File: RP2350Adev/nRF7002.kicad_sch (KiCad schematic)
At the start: 32 parts, among them U3 LFD_Diplexer, U4 nRF7002-QFAA, X3 XTAL-40

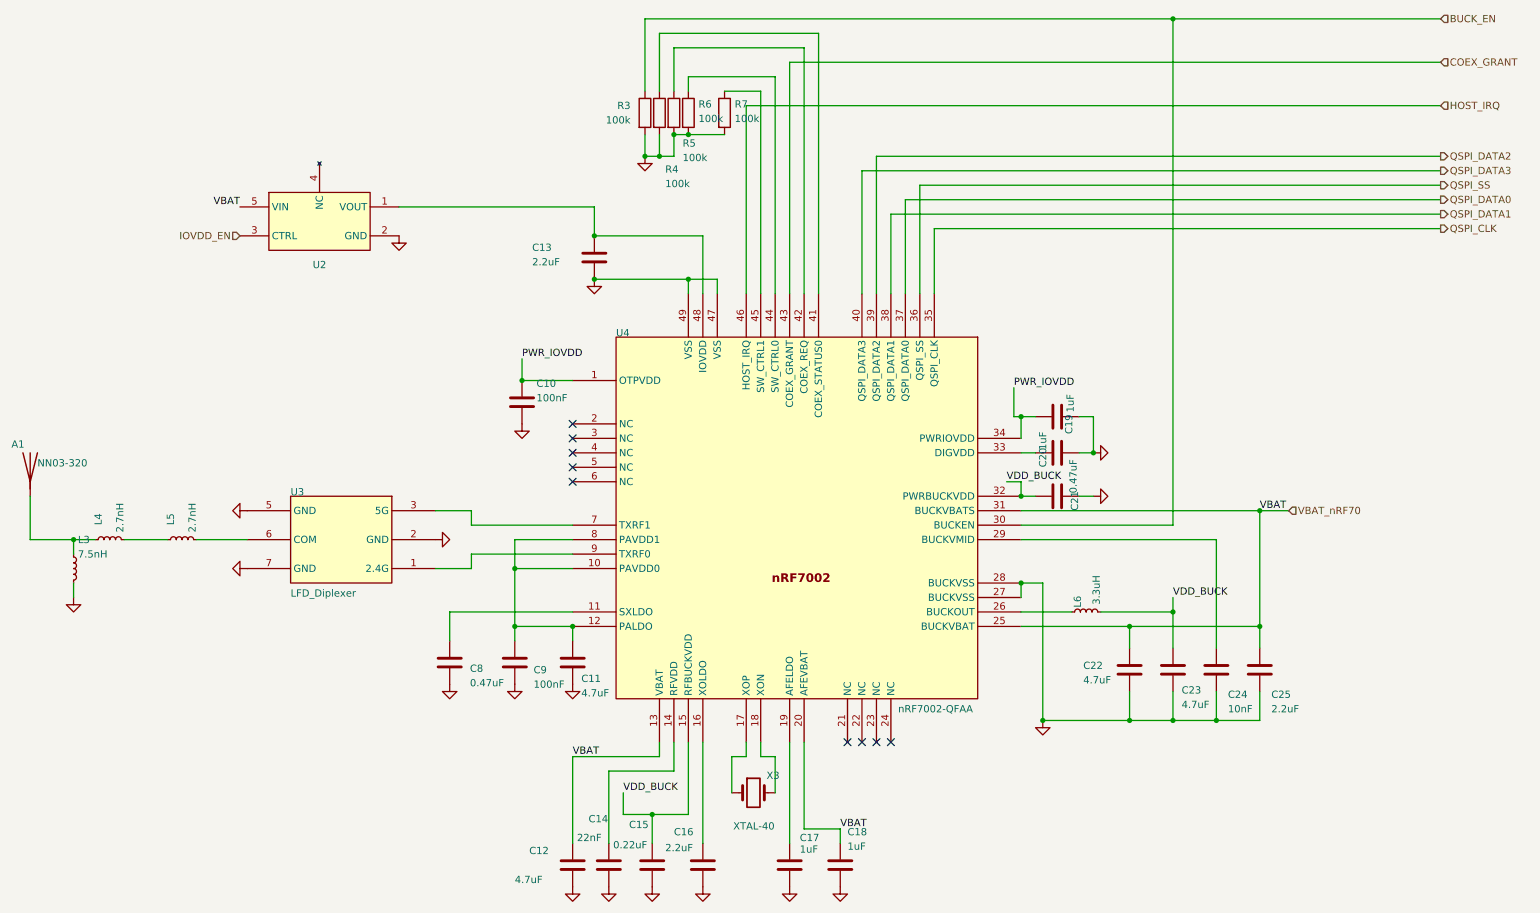
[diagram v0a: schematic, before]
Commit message: Layout Assembly Attempt (Components not being transferred as expected, major issues)
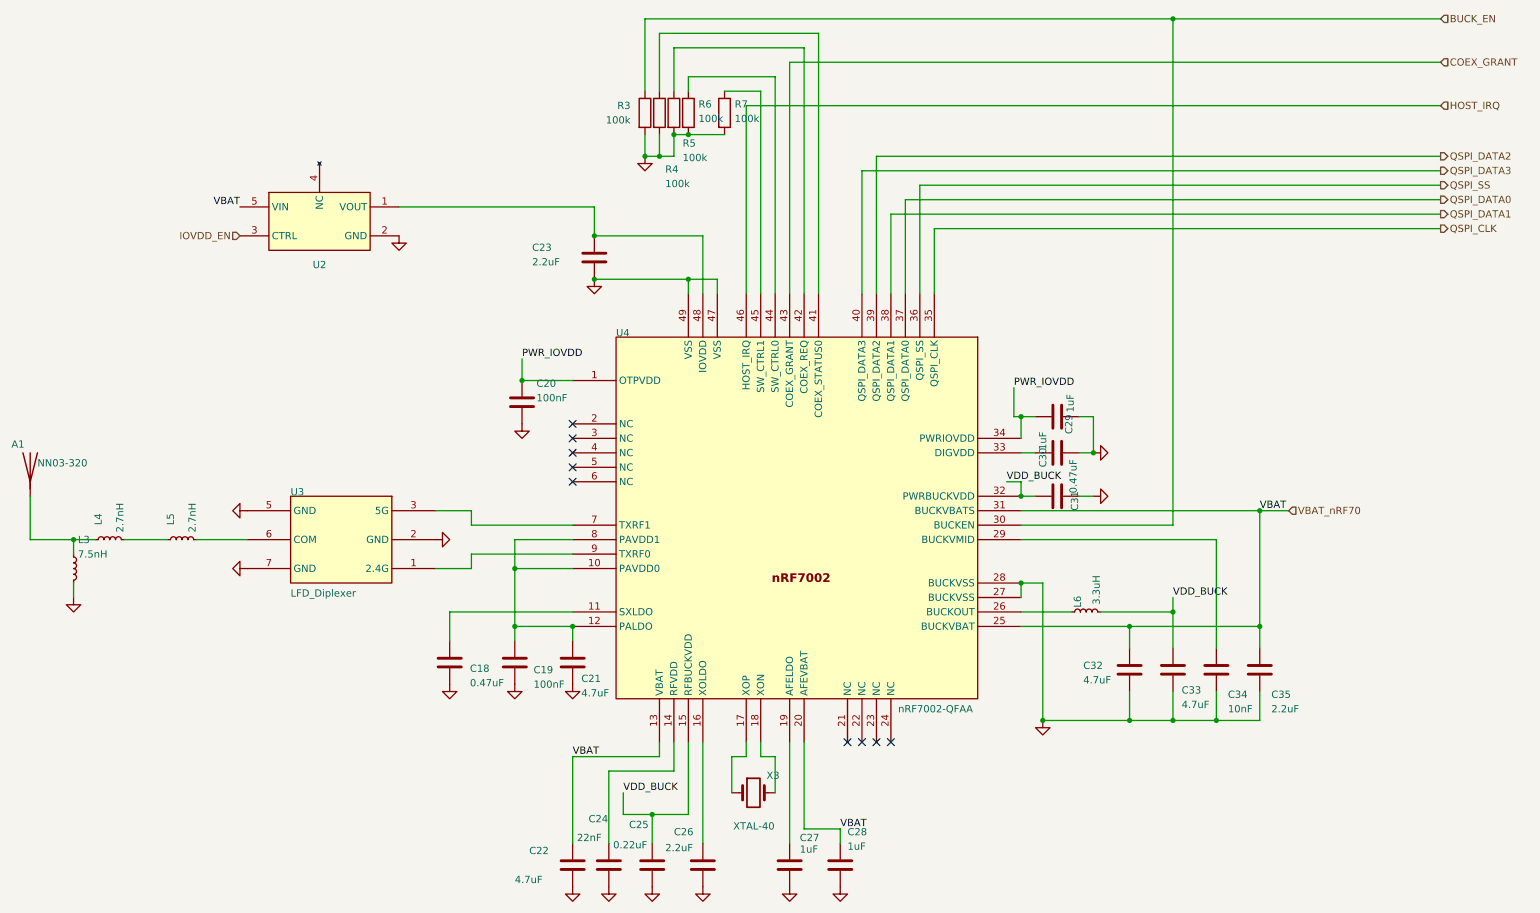
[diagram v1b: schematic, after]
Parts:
- renumbered C8 to C18, C9 to C19, C10 to C20, C11 to C21, C12 to C22, C13 to C23, C14 to C24, C15 to C25, C16 to C26, C17 to C27, C18 to C28, C19 to C29, C20 to C30, C21 to C31, C22 to C32, C23 to C33, C24 to C34, C25 to C35

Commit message: Combine subcircuits
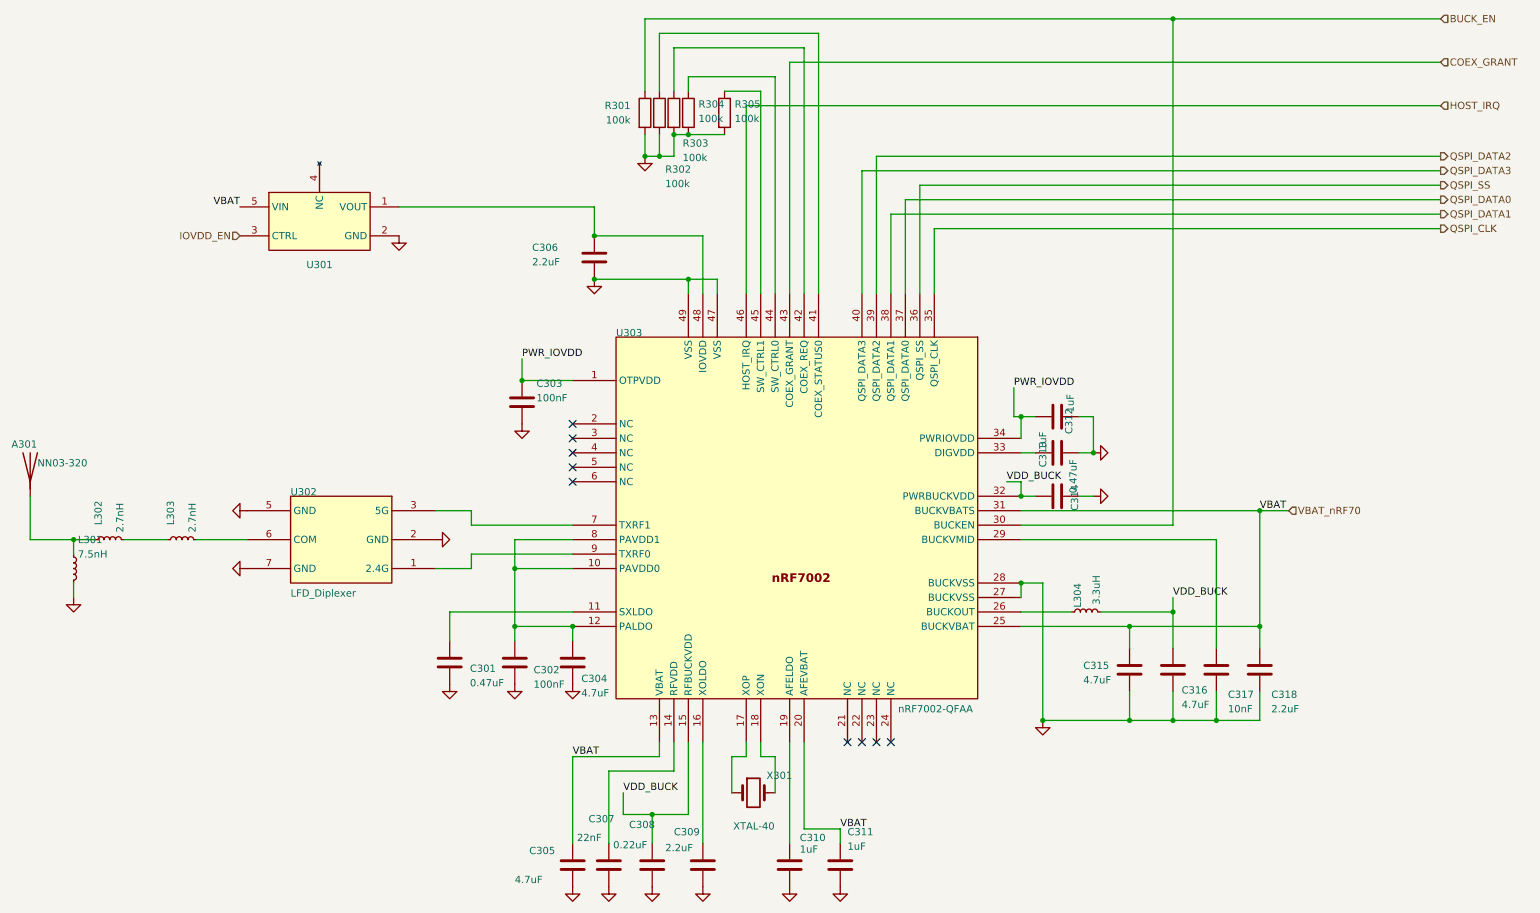
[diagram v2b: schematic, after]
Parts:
- renumbered A1 to A301, C18 to C301, C19 to C302, C20 to C303, C21 to C304, C22 to C305, C23 to C306, C24 to C307, C25 to C308, C26 to C309, C27 to C310, C28 to C311, C29 to C312, C30 to C313, C31 to C314, C32 to C315, C33 to C316, C34 to C317, C35 to C318, L3 to L301, L4 to L302, L5 to L303, L6 to L304, R3 to R301, R4 to R302, R5 to R303, R6 to R304, R7 to R305, U2 to U301, U3 to U302, U4 to U303, X3 to X301

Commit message: RF layout
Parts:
- A301: symbol Device:Antenna -> Device:Antenna_Shield
- U303: footprint Package_DFN_QFN:QFN-48-1EP_6x6mm_P0.4mm_EP4.66x4.66mm_ThermalVias -> Package_DFN_QFN:QFN-48-1EP_6x6mm_P0.4mm_EP4.6x4.6mm
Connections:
- no-connect marks 9 -> 10
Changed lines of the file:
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@@
 	)
 	(no_connect
+		(at 22.86 105.41)
+	)
+	(no_connect
 		(at 163.83 148.59)
 	)
@@
 	)
 	(symbol
-		(lib_id "Device:Antenna")
+		(lib_id "Device:Antenna_Shield")
 		(at 20.32 100.33 0)
 		(unit 1)
@@
 		)
 		(property "Footprint" "Eclectronics:XCVR_NN03-320"
-			(at 20.32 100.33 0)
+			(at 20.32 97.79 0)
 			(effects
 				(font
@@
 		)
 		(property "Datasheet" "~"
-			(at 20.32 100.33 0)
+			(at 20.32 97.79 0)
 			(effects
 				(font
@@
 			)
 		)
-		(property "Description" "Antenna"
+		(property "Description" "Antenna with extra pin for shielding"
 			(at 20.32 100.33 0)
 			(effects
@@
 		(pin "1"
 		)
+		(pin "2"
+		)
 		(instances
 			(project "main"
@@
 			)
 		)
-		(property "Footprint" "Package_DFN_QFN:QFN-48-1EP_6x6mm_P0.4mm_EP4.66x4.66mm_ThermalVias"
+		(property "Footprint" "Package_DFN_QFN:QFN-48-1EP_6x6mm_P0.4mm_EP4.6x4.6mm"
 			(at 123.19 77.47 0)
 			(effects

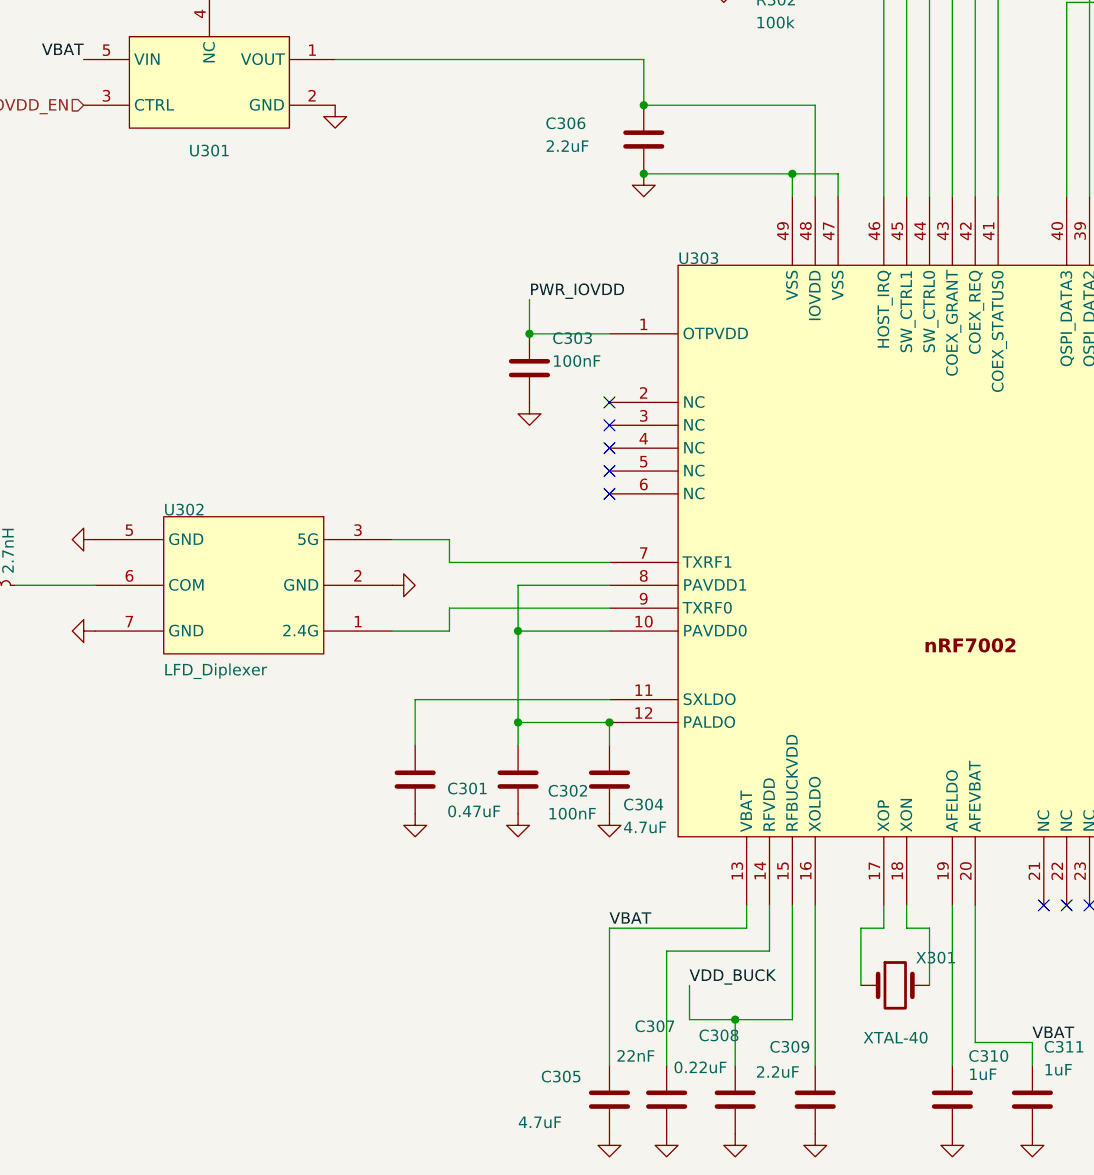
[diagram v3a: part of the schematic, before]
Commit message: fix footprint errors
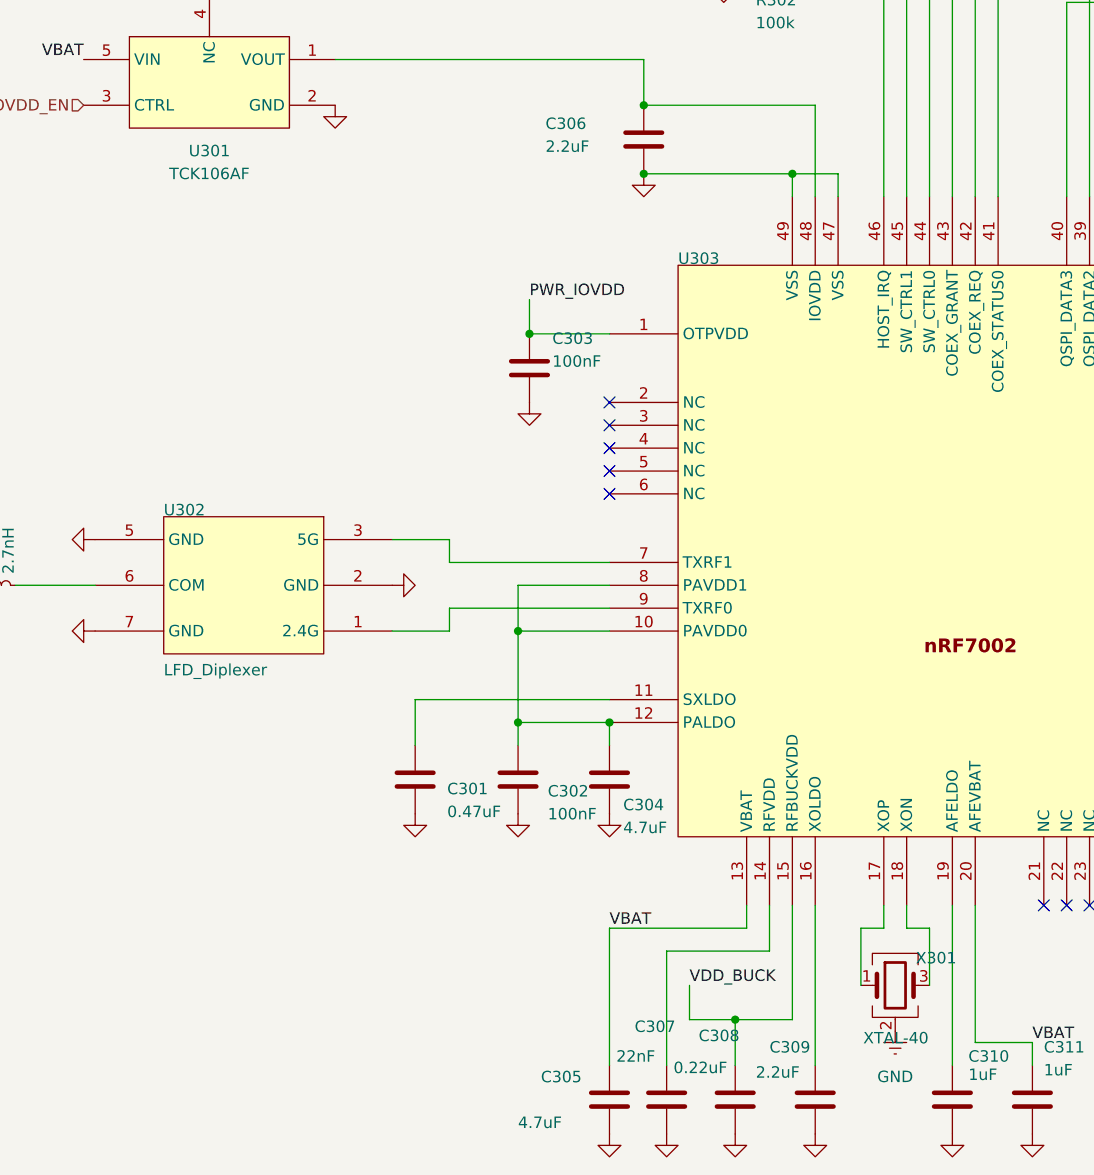
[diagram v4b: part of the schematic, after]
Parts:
- U301: value ~ -> TCK106AF
- X301: footprint Crystal:Crystal_SMD_Abracon_ABM3-2Pin_5.0x3.2mm -> Eclectronics:XTAL_ABM11W-32.0000MHZ-8-D1X-T3; symbol Device:Crystal -> Device:Crystal_GND24
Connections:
- net GND: now also X301.2 (G), X301.4 (G)
- net at U303.18 (XON): now also X301.3; no longer X301.2
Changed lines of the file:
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@@
 			)
 		)
-		(property "Value" "~"
+		(property "Value" "TCK106AF"
 			(at 71.12 67.31 0)
 			(effects
@@
 	)
 	(symbol
+		(lib_id "power:GNDREF")
+		(at 147.32 162.56 0)
+		(unit 1)
+		(exclude_from_sim no)
+		(in_bom yes)
+		(on_board yes)
+		(dnp no)
+		(fields_autoplaced yes)
+		(property "Reference" "#PWR0321"
+			(at 147.32 168.91 0)
+			(effects
+				(font
+					(size 1.27 1.27)
+				)
+				(hide yes)
+			)
+		)
+		(property "Value" "GND"
+			(at 147.32 167.64 0)
+			(effects
+				(font
+					(size 1.27 1.27)
+				)
+			)
+		)
+		(property "Footprint" ""
+			(at 147.32 162.56 0)
+			(effects
+				(font
+					(size 1.27 1.27)
+				)
+				(hide yes)
+			)
+		)
+		(property "Datasheet" ""
+			(at 147.32 162.56 0)
+			(effects
+				(font
+					(size 1.27 1.27)
+				)
+				(hide yes)
+			)
+		)
+		(property "Description" "Power symbol creates a global label with name \"GNDREF\" , reference supply ground"
+			(at 147.32 162.56 0)
+			(effects
+				(font
+					(size 1.27 1.27)
+				)
+				(hide yes)
+			)
+		)
+		(pin "1"
+		)
+		(instances
+			(project "main"
+				(path "/1f57b86c-11e7-4ea8-8f36-592c0861a25b/136a9d44-a364-48e6-8424-e71f46d06146"
+					(reference "#PWR0321")
+					(unit 1)
+				)
+			)
+		)
+	)
+	(symbol
 		(lib_id "power:GND")
 		(at 105.41 138.43 0)
@@
 	)
 	(symbol
-		(lib_id "Device:Crystal")
+		(lib_id "Device:Crystal_GND24")
 		(at 147.32 157.48 0)
 		(unit 1)
@@
 			)
 		)
-		(property "Footprint" "Crystal:Crystal_SMD_Abracon_ABM3-2Pin_5.0x3.2mm"
+		(property "Footprint" "Eclectronics:XTAL_ABM11W-32.0000MHZ-8-D1X-T3"
 			(at 147.32 157.48 0)
 			(effects
@@
 			)
 		)
-		(property "Description" "Two pin crystal"
+		(property "Description" "Four pin crystal, GND on pins 2 and 4"
 			(at 147.32 157.48 0)
 			(effects
@@
 		(pin "2"
 		)
-		(instances
+		(pin "3"
+		)
+		(pin "4"
+		)
+		(instances
